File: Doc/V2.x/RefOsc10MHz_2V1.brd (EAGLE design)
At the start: 90 x 70 mm, 81 parts, among them CON1 TYCO-AMP_USBUSB-B_SMT, CON2 HEADER-2X5SMD, CON3 SD-73100-0105, CON4 AVR-ISP-6SMD, CON5 AVR-JTAG-10SMD, CON6 HEADER-2X3SMD, CON7 MCX-J-P-X-RA-SM1, IC1 ATmega328-P, IC2 LC4032V_XXT44, IC3 74HCT221D, IC6 LM2831YMF, IC7 CFPT-141, IC8 712-RXM-GNSS-TM-B, U5 OPA354

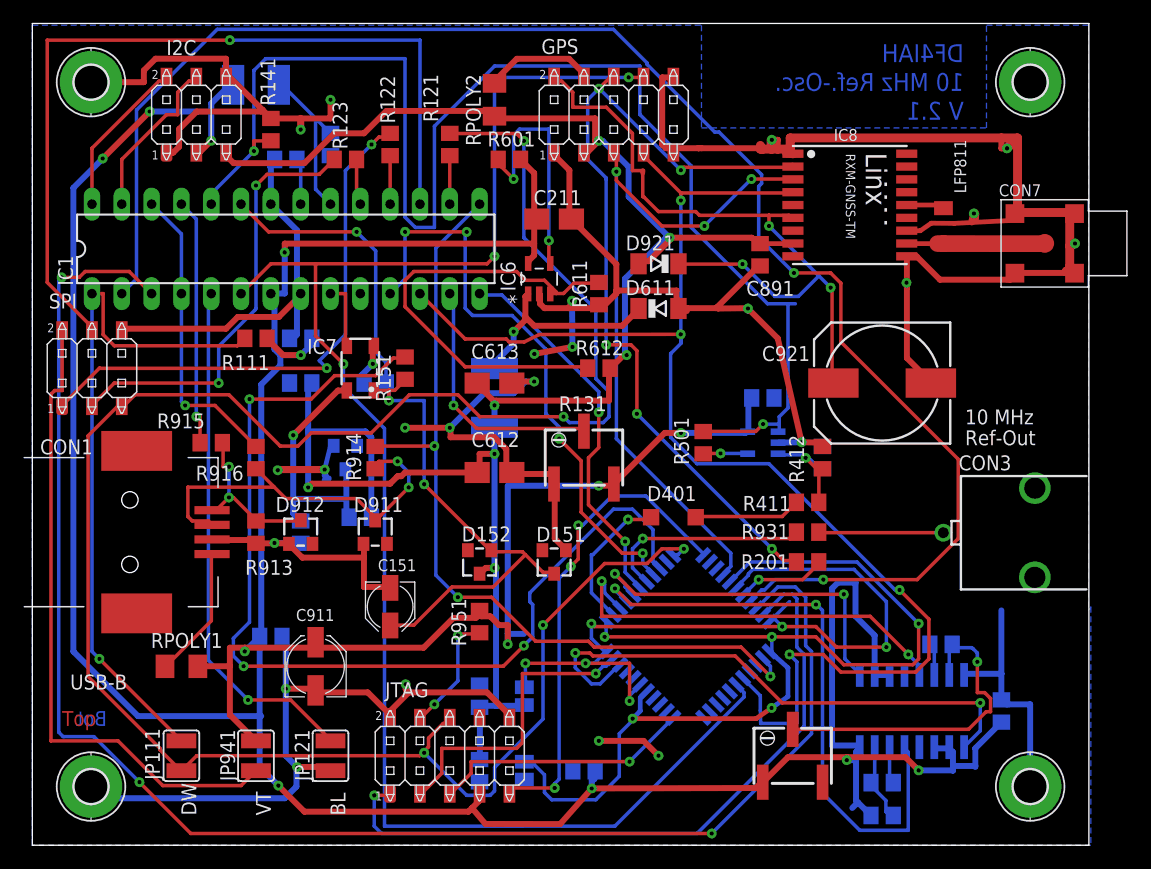
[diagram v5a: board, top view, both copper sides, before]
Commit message: avr_DF4IAH_Bootloader - Doc - Eagle: V2.1 - PWM pull signal via CPLD for clamping signals to defined values. AVR controller @ USB is not voltage regulated, the PWM output is therefore variable in its output voltage
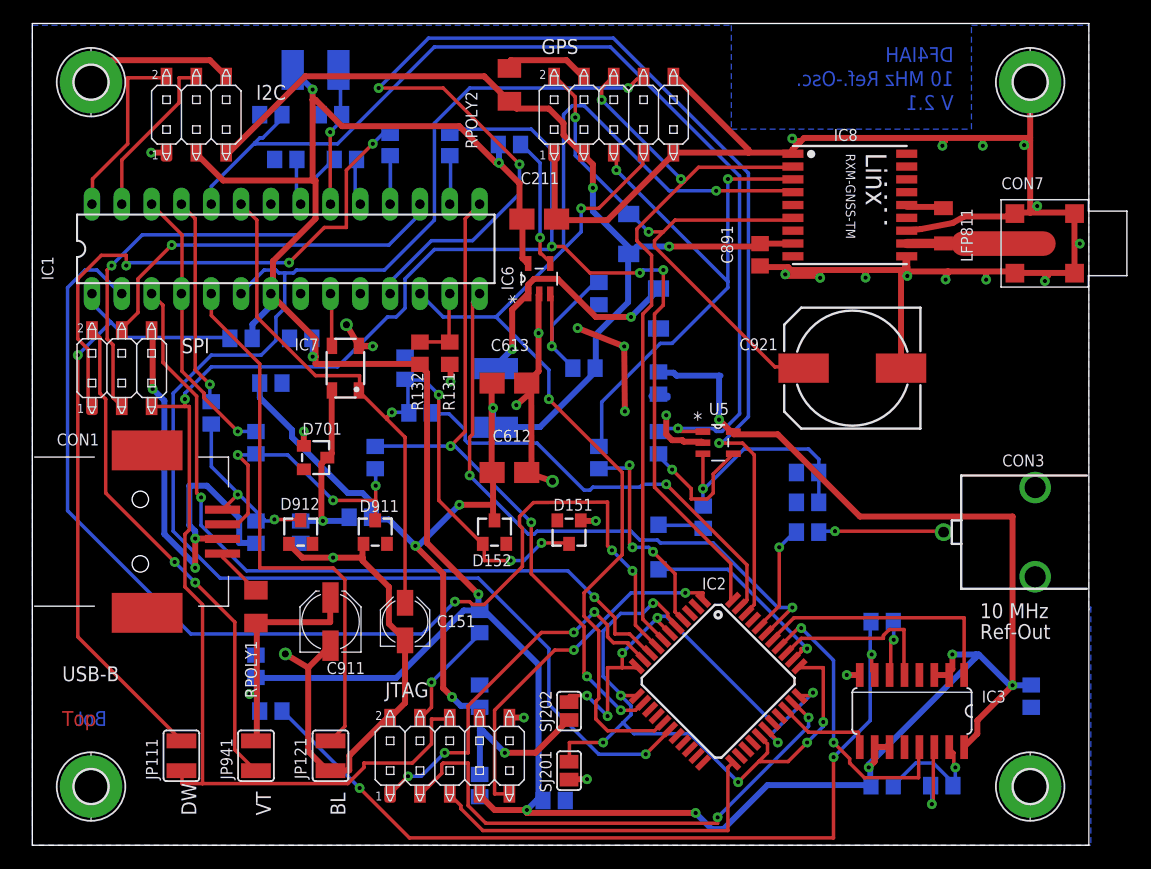
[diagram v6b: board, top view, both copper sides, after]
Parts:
- added R132: 47k, rcl:R0805
- R131: value 50k -> 15k; device df4iah:RTRIMTS63Y -> rcl:R0805
- R311: value 10k -> 4.7k; device df4iah:RTRIMTS63Y -> rcl:R0805
- moved R311 44.6 mm to (20.3, 11.4), flipped to the bottom
- moved R201 19.9 mm to (48.3, 33.0), flipped to the bottom, turned to 270 degrees
- moved R131 14.5 mm to (35.6, 41.9), turned to 90 degrees
- moved R411 8.98 mm to (57.1, 27.9), flipped to the bottom, turned to 90 degrees
- moved C591 8.98 mm to (53.3, 39.4), turned to 270 degrees
- moved RPOLY1 8.13 mm to (19.1, 20.3), turned to 270 degrees
- moved C311 5.38 mm to (72.4, 19.1), turned to 0 degrees
- moved L101 5.24 mm to (24.1, 66.0)
- moved C301 5.09 mm to (77.5, 5.08), turned to 180 degrees
- moved IC2 4.58 mm to (58.4, 14.0), flipped to the top
- moved R151 4.02 mm to (33.0, 36.8), flipped to the bottom, turned to 0 degrees
- moved SJ202 4.02 mm to (45.7, 11.4), flipped to the top
- moved C411 4.02 mm to (66.0, 29.2), turned to 0 degrees
- moved C911 4.02 mm to (25.4, 19.1)
- moved SJ201 3.81 mm to (45.7, 6.35), flipped to the top
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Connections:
- removed net CPLD_GPS_NMEA_TX: IC2.7, R201.2
- new net CPLD_GPS_NMEA_RX: IC2.4, R201.2
- net AIN1: now also R132.1
- net GPS_NMEA_RX: now also R201.1; no longer IC2.4
- net GPS_NMEA_TX: now also IC2.7; no longer R201.1
- net N$44: now also R311.1; no longer R311.2
- net VCC: now also R132.2, R311.2; no longer R131.3, R311.1
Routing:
- net GND: track 392.8 -> 292.6 mm, vias 24 -> 34
- net MCU_TXD: track 135.9 -> 65.0 mm, vias 3 -> 2
- net VCC: track 360.7 -> 297.3 mm, vias 13 -> 11
- net N_PWM_PULL_5V0: track 49.8 -> 111.7 mm, vias 4 -> 3
- net N_PWM_PULL_3V3: track 85.6 -> 37.1 mm, vias 3 -> 1
- net N$44: track 28.6 -> 73.2 mm, vias 1 -> 3
- net MCU_RXD: track 137.4 -> 97.1 mm, vias 2 -> 3
- net ISP_MOSI: track 72.0 -> 32.1 mm
- net GATE_TRIG_OUT: track 46.9 -> 8.34 mm, vias 2 -> 0
- net GND_SJ1: track 90.4 -> 56.6 mm, vias 5 -> 6
- net ADC_PHASE: track 118.3 -> 89.8 mm, vias 2 -> 1
- net VCC_3V3_SJ2: track 69.7 -> 42.2 mm
- net JTAG_TCK: track 59.6 -> 32.7 mm, vias 1 -> 4
- net SYNC_IN: track 51.4 -> 24.7 mm
- net FB: track 38.6 -> 14.5 mm, vias 0 -> 1
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
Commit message: avr_DF4IAH_Bootloader - Doc - Eagle: V2.1 - LcdModule-16x2_1V0 added, updates for RefOsc10MHz_2V1 also
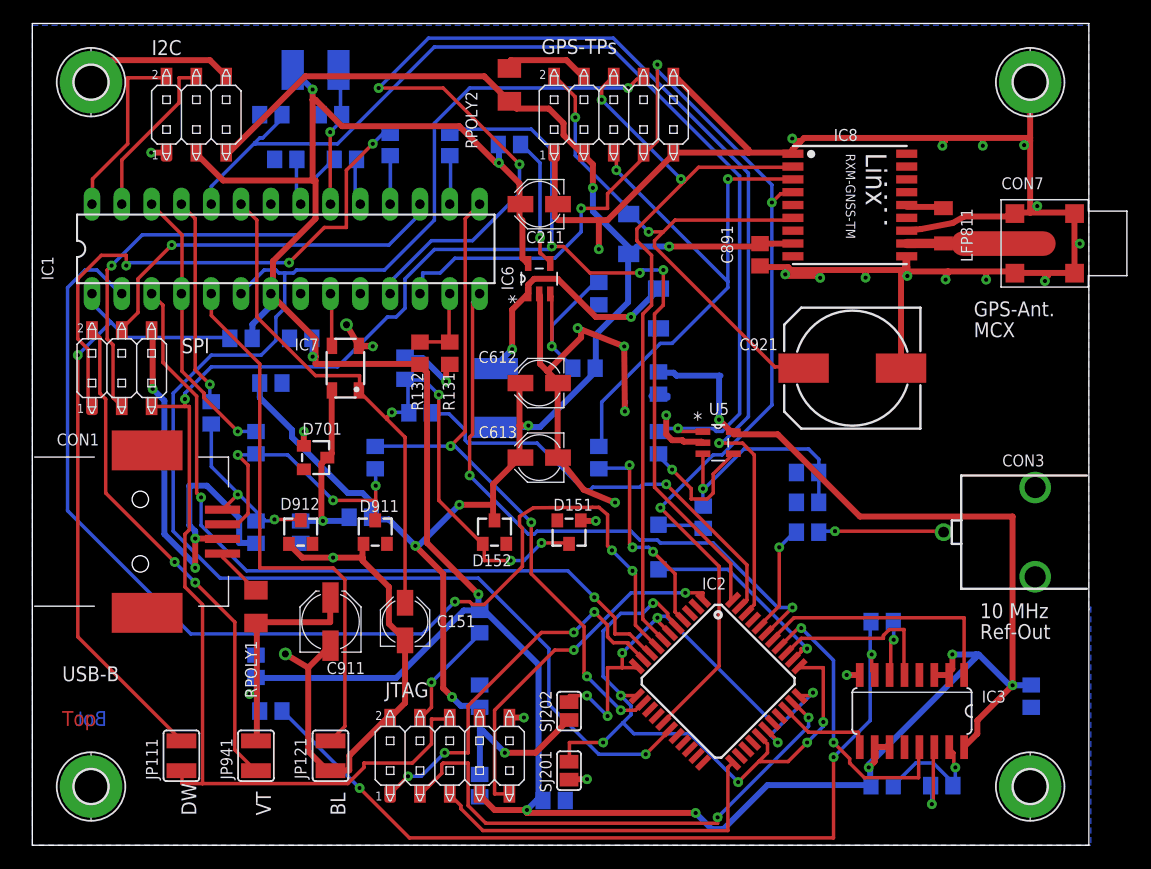
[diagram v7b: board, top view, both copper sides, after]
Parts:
- C211, C612, C613: device rcl:A/3216-18W -> rcl:PANASONIC_B
- moved C612 8.03 mm to (43.2, 39.4)
- moved C613 6.84 mm to (43.2, 33.0)
- moved C211 1.27 mm to (43.2, 54.6)
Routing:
- net GND: track 292.6 -> 306.0 mm, vias 34 -> 33
- net GPS_PPS: track 109.0 -> 106.0 mm, vias 3 -> 4
- net MCU_RXD: track 97.1 -> 96.0 mm
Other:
- board text added: "GPS-Ant. MCX"
- board text added: "GPS-TPs"
- board text removed: "GPS"

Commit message: avr_DF4IAH_Bootloader - Doc - Eagle: V2.1 - correction: CRS80 --> CRS08
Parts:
- D611, D921: value CRS80 -> CRS08
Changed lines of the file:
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@@
 <attribute name="VALUE" x="63.498440625" y="41.676578125" size="1.016" layer="27" rot="R180"/>
 </element>
-<element name="D611" library="diode" package="SOD80C" value="CRS80" x="53.34" y="45.72" smashed="yes" rot="MR270">
+<element name="D611" library="diode" package="SOD80C" value="CRS08" x="53.34" y="45.72" smashed="yes" rot="MR270">
 <attribute name="NAME" x="54.69835" y="43.927128125" size="1.016" layer="26" rot="MR90"/>
 <attribute name="VALUE" x="51.4271875" y="43.8820125" size="0.762" layer="28" rot="MR90"/>
 </element>
-<element name="D921" library="diode" package="SOD80C" value="CRS80" x="50.8" y="52.07" smashed="yes" rot="MR270">
+<element name="D921" library="diode" package="SOD80C" value="CRS08" x="50.8" y="52.07" smashed="yes" rot="MR270">
 <attribute name="NAME" x="50.984778125" y="55.33564375" size="1.016" layer="26" rot="MR90"/>
 <attribute name="VALUE" x="48.84568125" y="50.2119375" size="0.762" layer="28" rot="MR90"/>
